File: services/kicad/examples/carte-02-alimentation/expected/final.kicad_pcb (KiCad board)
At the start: 2 copper layers, 55 x 40 mm, 12 parts, among them J1 IN_5V, J2 OUT, U1 AMS1117-3.3, U2 AMS1117-1.8

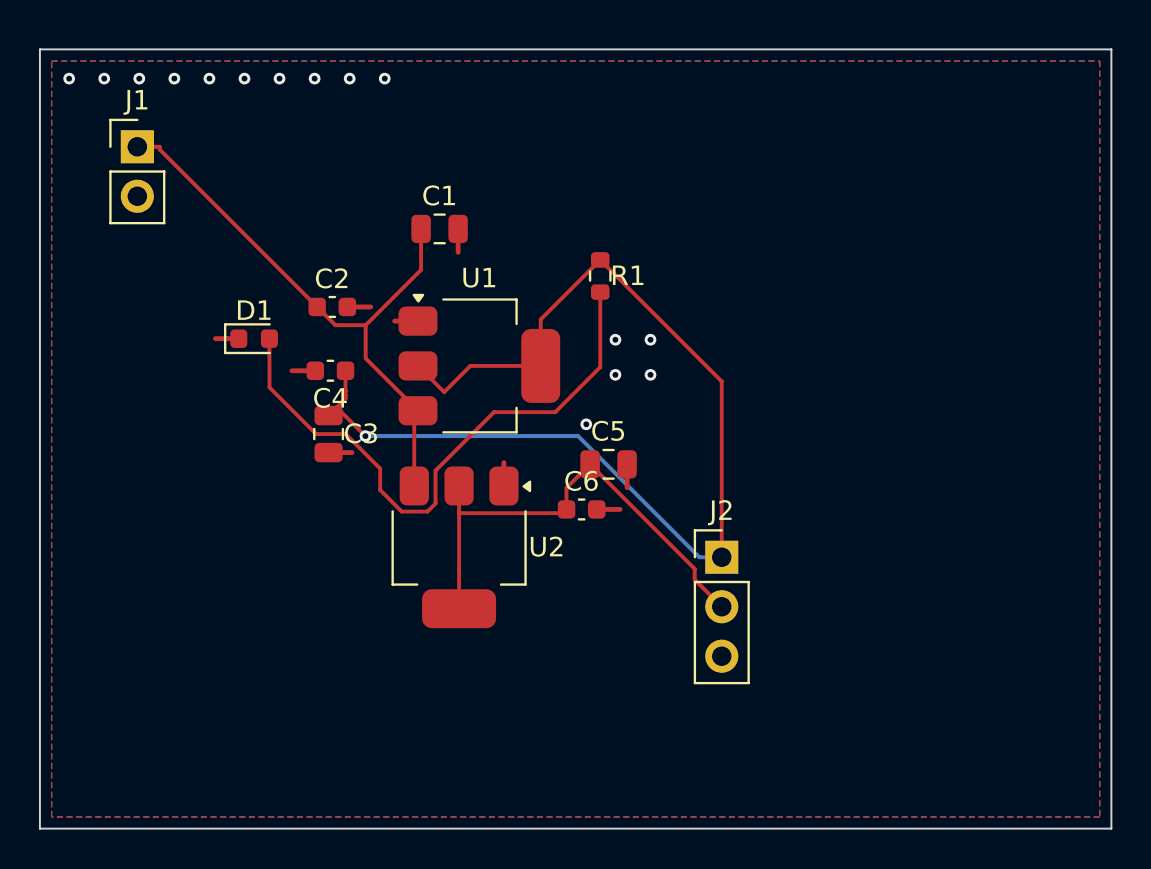
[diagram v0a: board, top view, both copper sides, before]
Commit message: feat(kicad): placement pro et routage 100 % fabricable sur les 16 cartes -- integration sur main (#164)
Branche d'integration coupee depuis origin/main (fab2a82, PR #162) : les
fichiers cles de main etaient des instantanes de feat/placement-seed-snap-
bypass (routing.py = 7981019, placement.py = 437a8b4...). On reprend donc
l'arbre entier de cette branche (345 commits, dernier 9f48667) et on y
conserve ce que main seul apportait :
- tools/verrou_routage.py + son test : « 6,2 Go par routage » rectifie
  (0,2 Go mesure ; c'est la concurrence qui emballe la memoire) ;
- tests/test_driver_llm_resync.py ;
- CLAUDE.md, PLAN.md, DECISIONS.md : fusion a trois voies, les sections
  des deux lignes conservees (2026-09-05 conteneur/verrou, 2026-09-07
  parcours asynchrone et chaine du driver, 2026-09-09/10 lecons).
Les skills *-delegate restent supprimes (remplaces le 2026-08-30).

Contenu : banc en deux phases (placement valide puis routage gele), snap
sur les regles natives, repli GND cible, journal Freerouting incremental,
horloge sans progres, via d'echappement vers le plan principal,
serigraphie degagee ; 16 cartes livrees a 100 %, 0 erreur DRC.

Verification : pytest services/kicad 1805 passed, 16 skipped ;
pnpm type-check 8/8.


Claude-Session: https://claude.ai/code/session_01TnMqm4La2CxQHHB5K8aSSV

Co-authored-by: Claude Fable 5.1 <noreply@anthropic.com>
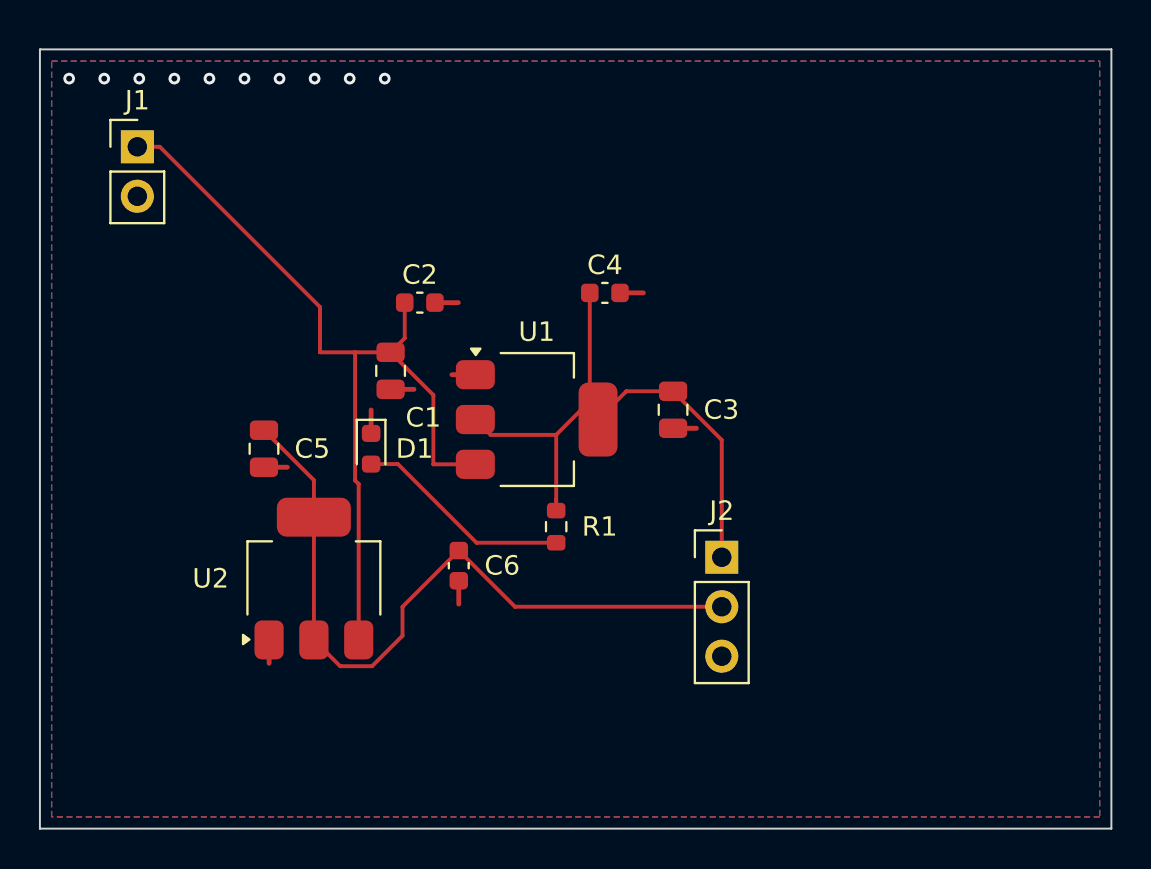
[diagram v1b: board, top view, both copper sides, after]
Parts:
- moved C3 17.7 mm to (153.5, 103.5)
- moved C5 17.7 mm to (132.5, 105.5), turned to -90 degrees
- moved C4 14.6 mm to (150.0, 97.5), turned to 0 degrees
- moved R1 13.1 mm to (147.5, 109.5)
- moved D1 8.24 mm to (138.0, 105.5), turned to -90 degrees
- moved C1 7.71 mm to (139.0, 101.5), turned to -90 degrees
- moved U2 7.62 mm to (135.1, 112.2), turned to 90 degrees
- moved C6 6.93 mm to (142.5, 111.5), turned to -90 degrees
- moved C2 4.50 mm to (140.5, 98.0)
- moved U1 4.03 mm to (146.5, 104.0)
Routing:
- net +3V3: track 57.6 -> 31.3 mm, vias 1 -> 0
- net LED_A: track 30.7 -> 11.2 mm
- net VIN: track 31.2 -> 45.2 mm
- net +1V8: track 24.8 -> 37.8 mm
- net GND: vias 15 -> 10

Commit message: chore(banc): relivrer carte-01..10 avec la couture corrigee
Boards reroutes par HTTP depuis placement.kicad_pcb inchange, avec le
code de #217. Juges par remesurer_banc.py : 0 erreur, 0 connexion
manquante sur les dix. 678 -> 443 vias ; la rangee de vias GND du bord
haut a disparu.

mesures.json : `board` recompte, `drc_du_board` rejuge, nouvelle cle
`couture_corrigee` (date, vias_avant, couches). journal.txt et les
champs du run d origine sont laisses tels quels et le disent.
rendu-3d.png : kicad-cli, modeles 3D, iso 1400x900.

Couches d un tirage : huit cartes sur 2, carte-08 et carte-10 sur 4.
CLAUDE.md et BANC_DRIVER_LLM.md recomptes. carte-11 non touchee.

Co-Authored-By: Claude Opus 5 (1M context) <noreply@anthropic.com>
Claude-Session: https://claude.ai/code/session_01TnMqm4La2CxQHHB5K8aSSV
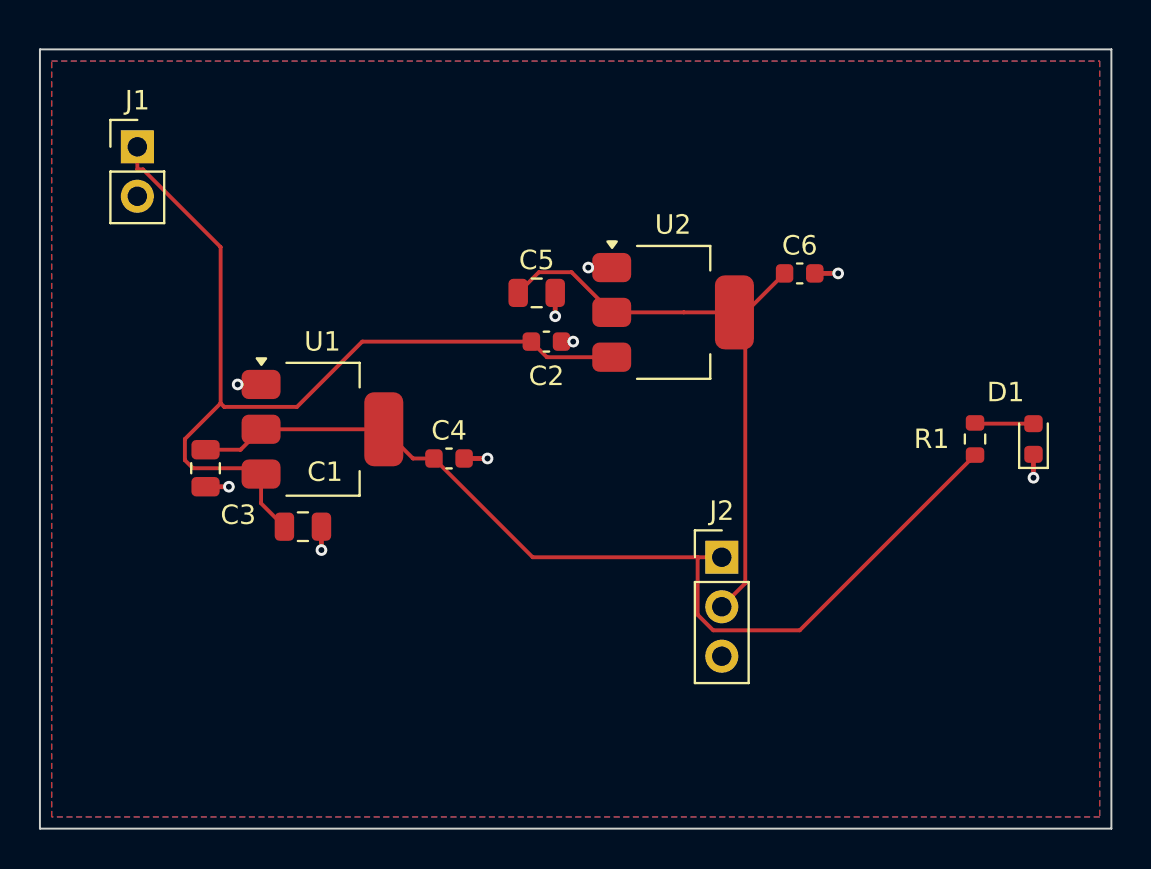
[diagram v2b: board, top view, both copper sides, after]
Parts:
- moved D1 34.0 mm to (172.0, 105.0), turned to 90 degrees
- moved C3 24.2 mm to (129.5, 106.5)
- moved C6 23.0 mm to (160.0, 96.5), turned to 0 degrees
- moved U2 22.9 mm to (153.5, 98.5), turned to 0 degrees
- moved R1 22.0 mm to (169.0, 105.0), turned to 90 degrees
- moved C5 16.1 mm to (146.5, 97.5), turned to 0 degrees
- moved C4 11.7 mm to (142.0, 106.0)
- moved U1 11.0 mm to (135.5, 104.5)
- moved C1 9.18 mm to (134.5, 109.5), turned to 0 degrees
- moved C2 6.80 mm to (147.0, 100.0)
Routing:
- net +3V3: track 31.3 -> 50.9 mm
- net LED_A: track 11.2 -> 3.02 mm
- net +1V8: track 37.8 -> 31.6 mm
- net VIN: track 45.2 -> 48.1 mm
- net GND: track 10.8 -> 10.2 mm, vias 10 -> 9

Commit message: chore(banc): relivrer carte-01/02/04/05 compactes (25 %, D-2026-09-20-a) (#222)
Chaine place -> route rejouee par HTTP sur les dix cartes avec le code de
#220/#221. Quatre sortent a 0 erreur et 0 connexion manquante, sur des
cartes 18 a 58 % plus petites :

  carte-01  24,8x17 -> 20x14      carte-02  55x40 -> 35x25
  carte-04  45x44,8 -> 39x30      carte-05  70x50 -> 46x33

placement.kicad_pcb et final.kicad_pcb remplaces ENSEMBLE ; mesures.json :
board recompte, drc_du_board rejuge (remesurer_banc.py), cle
carte_compacte (tailles et vias d avant, durees, moteur, pistes par
couche). Rendus refaits. Connecteurs a <= 5 mm d un bord (carte-02 J2 :
13,9 -> 3,8 mm) ; carte-05 J3 inchange a 11,4 mm (origine pin 1).

Les six autres gardent leur board du 2026-09-19 : 06 et 08 a 1 manquante,
03 et 07 mauvais, 09 et 10 sans board (tirages figes). Detail dans
BANC_DRIVER_LLM.md. carte-11 non touchee.


Claude-Session: https://claude.ai/code/session_01TnMqm4La2CxQHHB5K8aSSV

Co-authored-by: Claude Fable 5.1 <noreply@anthropic.com>
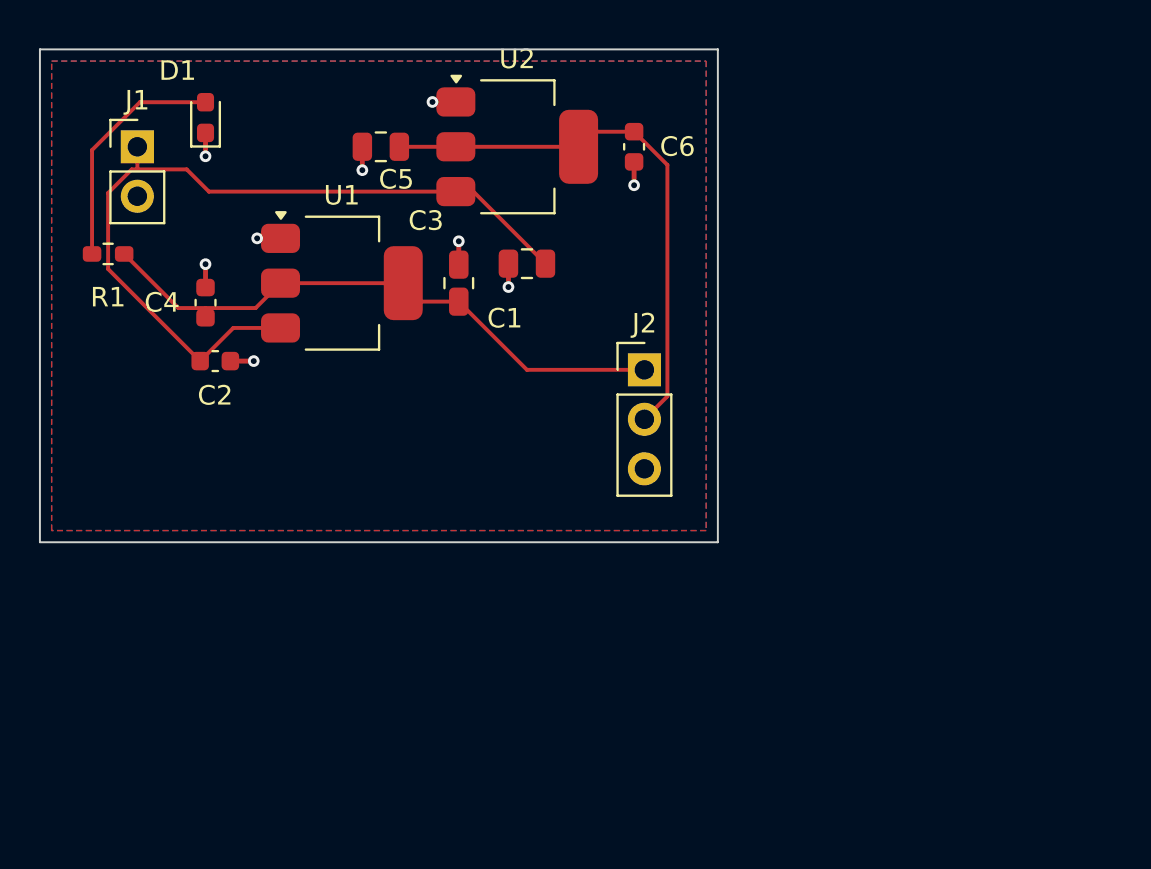
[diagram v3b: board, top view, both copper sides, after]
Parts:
- moved D1 45.6 mm to (129.5, 88.5)
- moved R1 45.5 mm to (124.5, 95.5), turned to 180 degrees
- moved C1 17.7 mm to (146.0, 96.0), turned to 180 degrees
- moved C2 17.0 mm to (130.0, 101.0)
- moved C3 16.1 mm to (142.5, 97.0), turned to 90 degrees
- moved C4 14.8 mm to (129.5, 98.0), turned to 90 degrees
- moved U2 11.7 mm to (145.5, 90.0)
- moved C5 11.0 mm to (138.5, 90.0), turned to 180 degrees
- moved C6 10.7 mm to (151.5, 90.0), turned to -90 degrees
- moved J2 10.4 mm to (152.0, 101.5)
- moved U1 7.57 mm to (136.5, 97.0)
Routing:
- net +3V3: track 50.9 -> 30.7 mm
- net LED_A: track 3.02 -> 12.2 mm
- net VIN: track 48.1 -> 41.5 mm
- net +1V8: track 31.6 -> 28.3 mm
- net GND: track 10.2 -> 10.8 mm
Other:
- board size 55 x 40 mm -> 34.8 x 25.3 mm

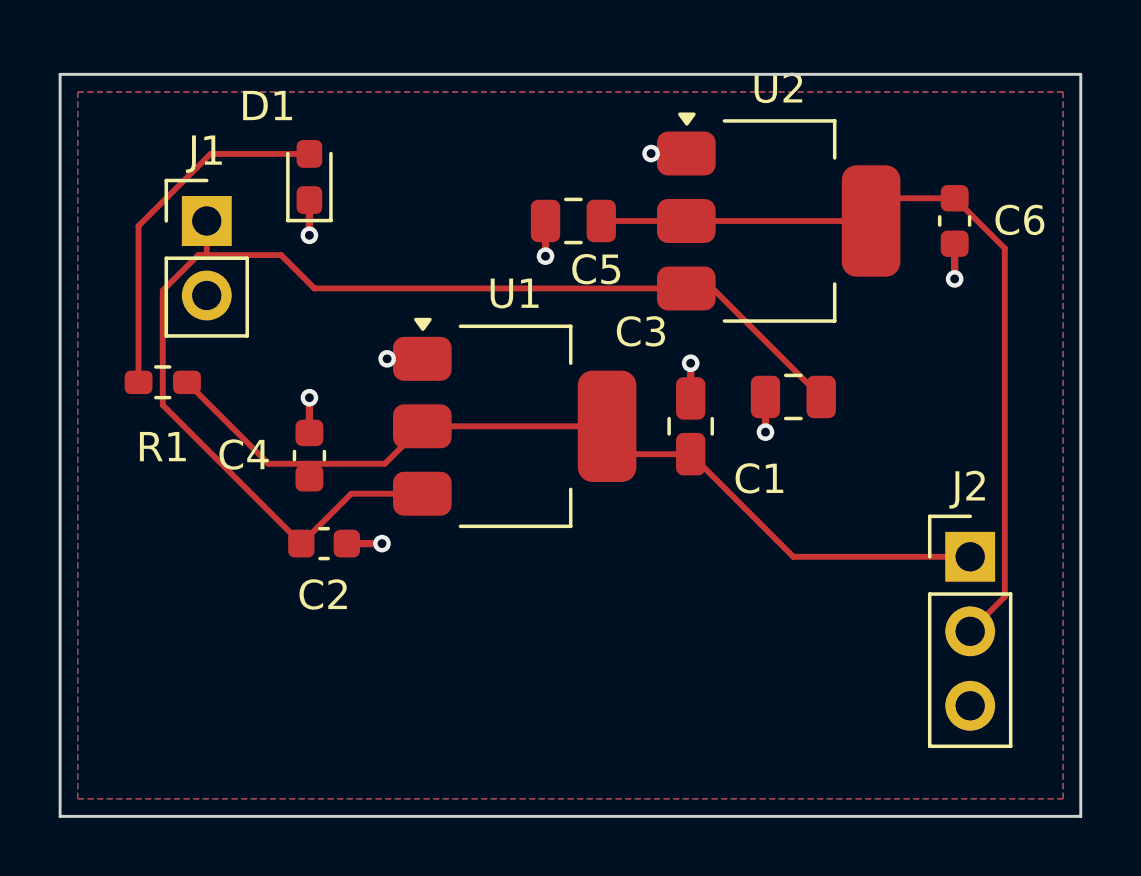
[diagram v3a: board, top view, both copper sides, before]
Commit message: fix(banc): le contour n etait JAMAIS resserre — dix cartes divisees par 2 a 4
Question de l utilisateur devant les rendus : « tu es satisfait de ce
placement ? ». Non, et la mesure lui donnait raison.

    carte-10 livree     140 x 105 mm = 14725 mm2
    son circuit          51 x  66 mm =  3366 mm2
    OCCUPATION                            23 %
    connecteurs                      56 a 75 mm du circuit
    fil de signal                      1230 mm  (VIN a lui seul 112 mm)

LA CAUSE : `run_pipeline.py` n envoyait pas `auto_size_board` a `/place/auto`.
Le resserrement du contour sur le placement existe depuis le 2026-09-13 et ne
s execute que si l appelant l autorise ; le defaut du modele est `False`.

C est le SEPTIEME levier de ce projet qui existe et que personne n appelle,
apres max_distance_mm, anchor_pin, WorkflowConfig.grid, constraints,
move_reference, bottom_up_placement et LocalRerouter.

⚠️ Et il etait INVISIBLE : la chaine de PRODUCTION passe bien le drapeau depuis
`handlePlacement`. Le banc mesurait donc un comportement que le produit n a
pas — l inverse exact de ce a quoi sert un banc.

MESURE APRES CORRECTION, meme circuit, meme graine :

    carte             demandee      REELLE        err  manq
    carte-01           25 x 20     20,1 x 14,6     0    0
    carte-02           55 x 40     34,9 x 25,4     0    0
    carte-03           50 x 35     26,1 x 20,1     0    0
    carte-04           60 x 45     36,6 x 27,2     0    0
    carte-05           70 x 50     43,6 x 32,6     0    0
    carte-06           80 x 60     48,5 x 36,4     0    0
    carte-07          110 x 80     53,2 x 38,8     0    0
    carte-08          125 x 95     56,4 x 44,1     0    0
    carte-09          130 x 100    57,3 x 45,2     0    0
    carte-10          140 x 105    61,0 x 45,8     0    0

Dix sur dix, 100 % route, aucune erreur, aucune connexion manquante. Sur
carte-10 : occupation 23 -> 56 %, fil de signal 1230 -> 652 mm, VIN 112 -> 45,5,
connecteurs 56-75 -> 23-35 mm.

ET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
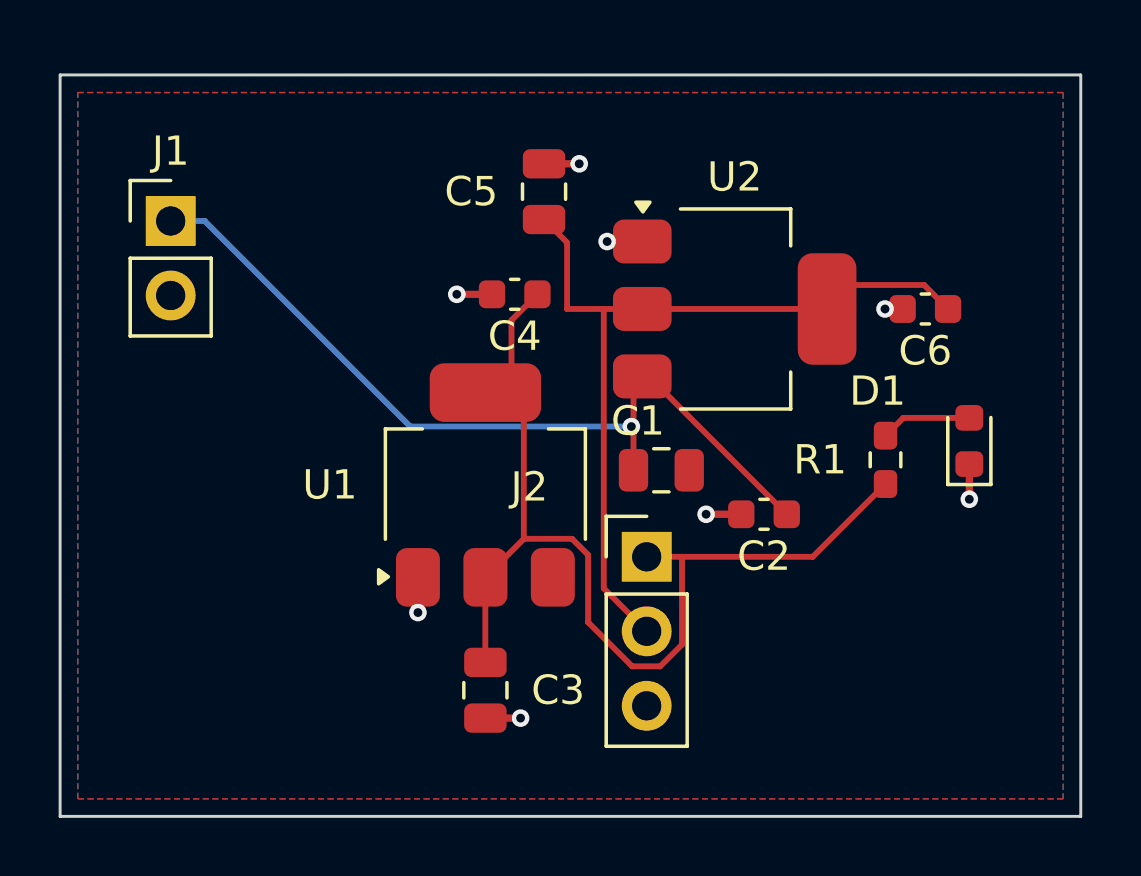
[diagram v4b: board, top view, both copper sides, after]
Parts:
- moved R1 24.8 mm to (149.1, 98.1), turned to 90 degrees
- moved D1 24.2 mm to (152.0, 97.5)
- moved C2 15.0 mm to (145.0, 100.0), turned to 180 degrees
- moved C3 11.4 mm to (135.5, 106.0), turned to -90 degrees
- moved J2 11.0 mm to (141.0, 101.5)
- moved C4 8.90 mm to (136.5, 92.5), turned to 180 degrees
- moved C1 5.15 mm to (141.5, 98.5), turned to 0 degrees
- moved U2 3.35 mm to (144.0, 93.0)
- moved C6 3.16 mm to (150.5, 93.0), turned to 180 degrees
- moved U1 2.24 mm to (135.5, 99.0), turned to 90 degrees
- moved C5 1.41 mm to (137.5, 89.0), turned to 90 degrees
- moved J1 1.23 mm to (124.8, 90.0)
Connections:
- U1 pad 3: VIN -> PWR_FLAG
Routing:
- net VIN: track 41.5 -> 28.9 mm, vias 0 -> 1
- net LED_A: track 12.2 -> 3.11 mm
- net +3V3: track 30.7 -> 35.5 mm
- net GND: track 10.8 -> 9.00 mm, vias 9 -> 8
